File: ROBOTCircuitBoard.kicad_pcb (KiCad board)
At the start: 2 copper layers, 27 parts, among them J3 CONN_01X02, P3 Pushbutton NO, P4 USB_OTG, U2 MK20DX256VLH7, U3 LP38691, U4 MKL02, Y1 Crystal 16MHz

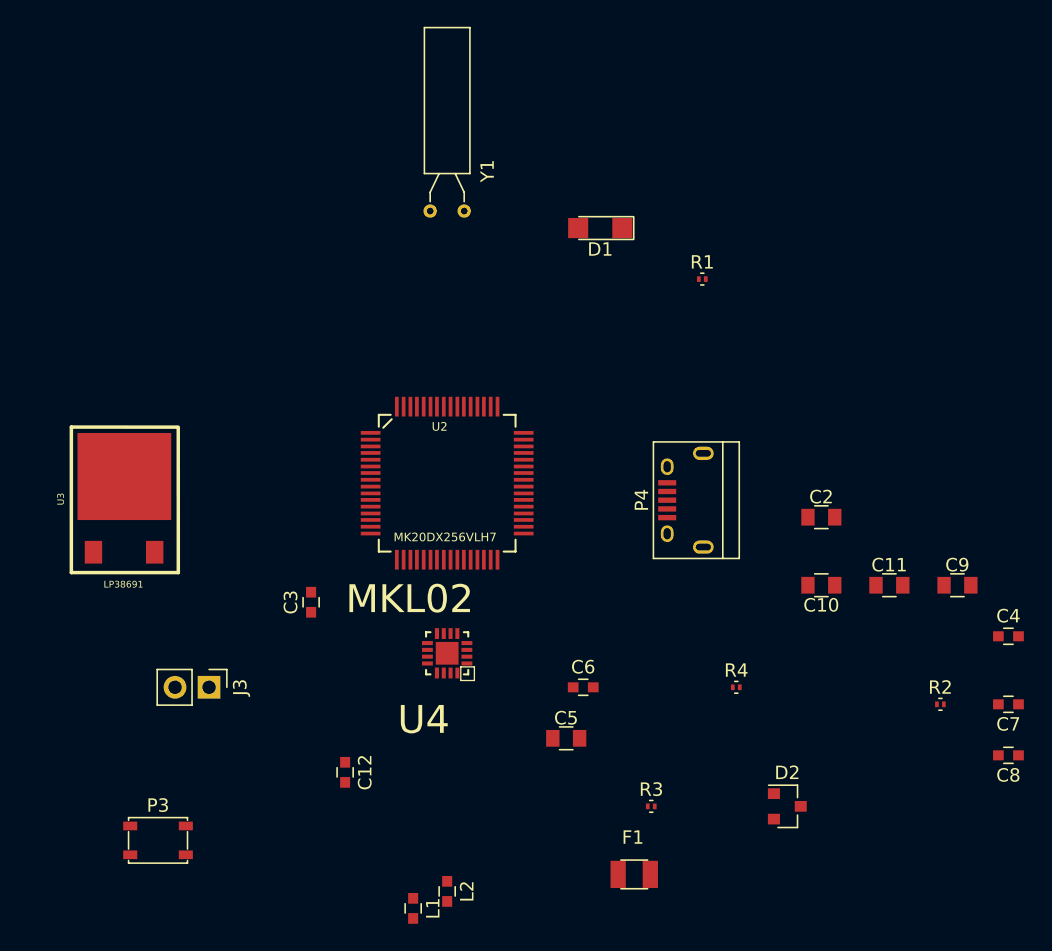
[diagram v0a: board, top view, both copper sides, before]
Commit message: updated netlist, soread out objects
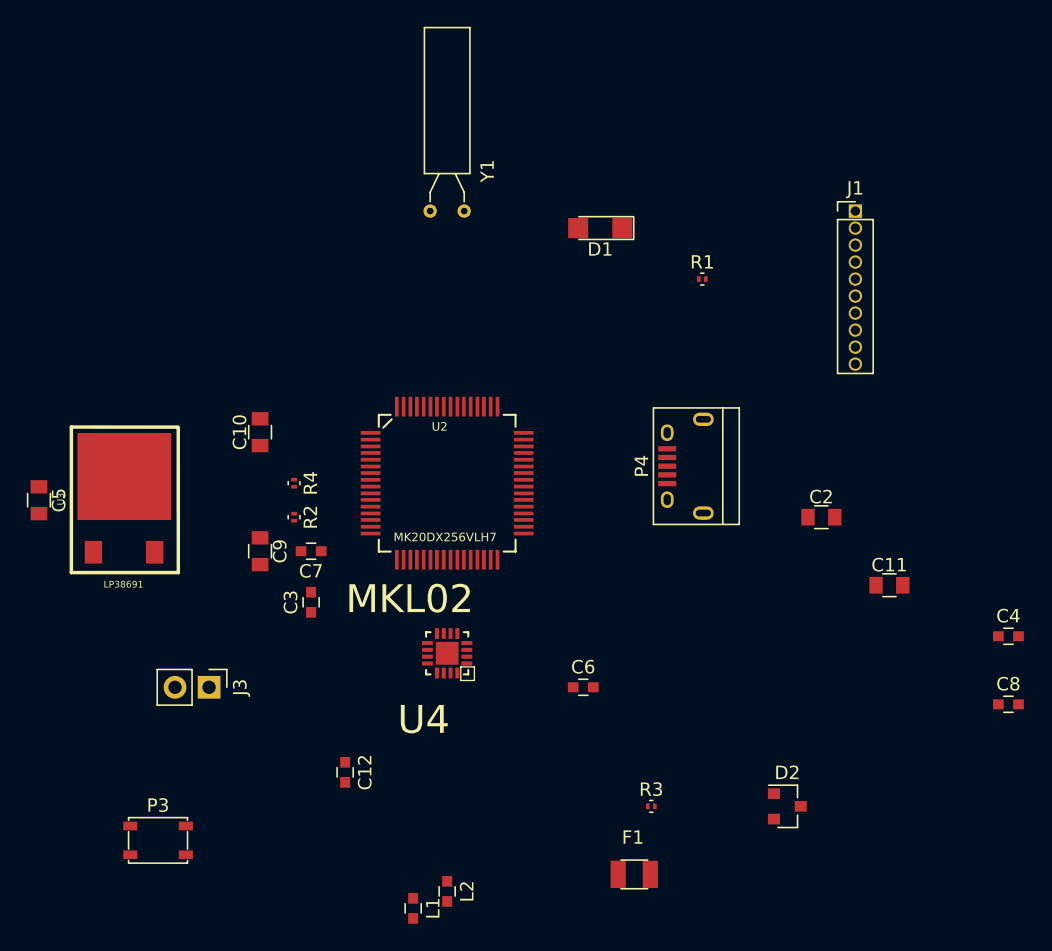
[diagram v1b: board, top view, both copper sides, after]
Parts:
- added J1: Analog 9-0, Socket_Strips:Socket_Strip_Straight_1x10_Pitch1.27mm, F.Cu at (163.8, 66.0)
- moved C7 53.3 mm to (123.2, 91.4)
- moved C9 52.1 mm to (119.4, 91.4), turned to 270 degrees
- moved R2 50.2 mm to (121.9, 88.9), turned to 270 degrees
- moved C10 43.4 mm to (119.4, 82.5), turned to 90 degrees
- moved C5 43.2 mm to (102.9, 87.6), turned to 270 degrees
- moved R4 36.4 mm to (121.9, 86.4), turned to 270 degrees
- moved C8 3.81 mm to (175.3, 102.9), turned to 0 degrees
- moved P4 2.54 mm to (151.1, 85.1)
